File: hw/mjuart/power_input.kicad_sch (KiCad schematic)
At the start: 11 parts, among them J2 USB4110-GF-A

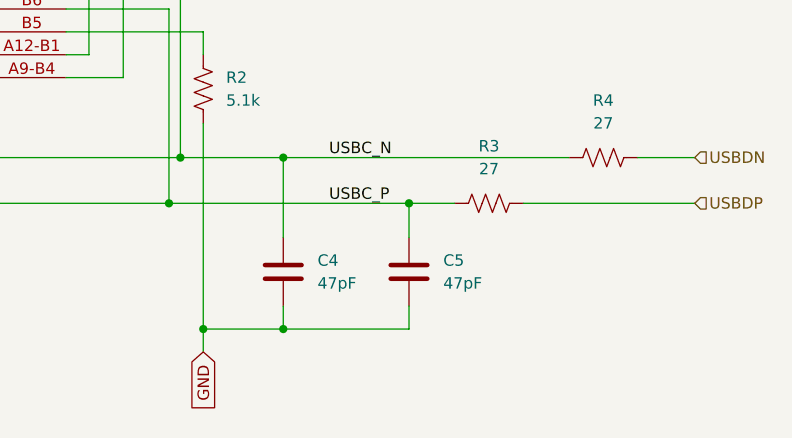
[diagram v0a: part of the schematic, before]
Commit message: mjuart: Fill in all BOM entries and slight layout tweaks
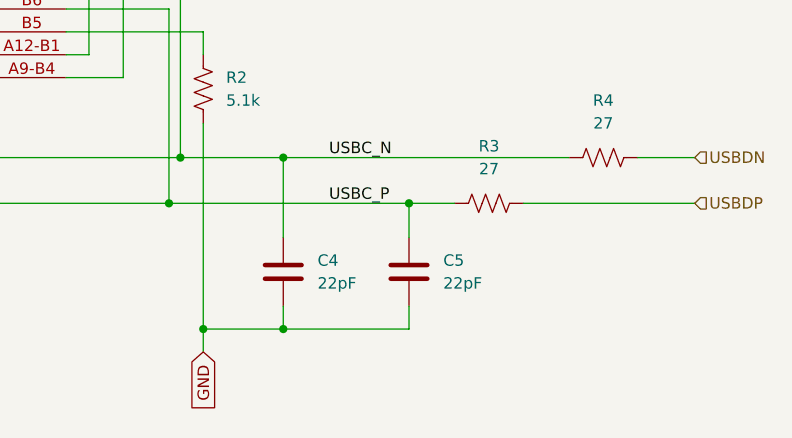
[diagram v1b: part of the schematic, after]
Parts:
- C1: MPN (none) -> MF-CAP-0603-0.01uF
- C2: MPN (none) -> MF-CAP-0603-0.1uF
- C3: MF (none) -> Murata; MPN (none) -> GRT188C81E475KE13D
- C4, C5: value 47pF -> 22pF; MPN (none) -> MF-CAP-0603-22pF
- R3, R4: MPN (none) -> MF-RES-0603-27
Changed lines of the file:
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@@
 			)
 		)
-		(property "MPN" ""
+		(property "MPN" "MF-CAP-0603-0.01uF"
 			(at 129.54 74.93 0)
 			(effects
@@
 			)
 		)
-		(property "MPN" ""
+		(property "MPN" "MF-RES-0603-27"
 			(at 177.8 106.68 0)
 			(effects
@@
 			)
 		)
-		(property "Value" "47pF"
+		(property "Value" "22pF"
 			(at 160.02 120.6499 0)
 			(effects
@@
 			)
 		)
-		(property "MPN" ""
+		(property "MPN" "MF-CAP-0603-22pF"
 			(at 156.21 119.38 0)
 			(effects
@@
 			)
 		)
-		(property "MPN" ""
+		(property "MPN" "GRT188C81E475KE13D"
+			(at 158.75 74.93 0)
+			(effects
+				(font
+					(size 1.27 1.27)
+				)
+				(hide yes)
+			)
+		)
+		(property "MF" "Murata"
 			(at 158.75 74.93 0)
 			(effects
@@
 			)
 		)
-		(property "MPN" ""
+		(property "MPN" "MF-CAP-0603-0.1uF"
 			(at 146.05 74.93 0)
 			(effects
@@
 			)
 		)
-		(property "MPN" ""
+		(property "MPN" "MF-RES-0603-27"
 			(at 165.1 111.76 0)
 			(effects
@@
 			)
 		)
-		(property "Value" "47pF"
+		(property "Value" "22pF"
 			(at 146.05 120.6499 0)
 			(effects
@@
 			)
 		)
-		(property "MPN" ""
+		(property "MPN" "MF-CAP-0603-22pF"
 			(at 142.24 119.38 0)
 			(effects

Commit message: mjuart: Fix all ERC and DRC violations
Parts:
- J2: symbol fdcanusb:USB4110-GF-A -> mjuart:USB4110-GF-A
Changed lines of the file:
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@@
 	)
 	(symbol
-		(lib_id "fdcanusb:USB4110-GF-A")
+		(lib_id "mjuart:USB4110-GF-A")
 		(at 77.47 85.09 0)
 		(unit 1)
@@
 					(size 1.27 1.27)
 				)
+				(hide yes)
 			)
 		)

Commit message: mjuart: Fix ZH4 pinout to match moteus-r4
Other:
- title: mjuart r1 -> mjuart r2
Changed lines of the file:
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@@
 	(paper "A4")
 	(title_block
-		(title "mjuart r1")
+		(title "mjuart r2")
 		(company "mjbots Robotic Systems, LLC - info@mjbots.com")
 		(comment 1 "Licensed under the Apache 2.0 License")
